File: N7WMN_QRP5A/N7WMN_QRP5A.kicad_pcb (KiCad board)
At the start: 4 copper layers, 159 x 159 mm, 468 parts, among them IC1 SN74CBTLV3253, J1 Conn_01x02, J10 Conn_01x03, J13 Conn_01x02, J14 Conn_01x04, J15 Conn_01x08, J16 Conn_01x03, J17 Conn_01x10, J18 Conn_01x10, J2 Conn_01x02, J3 Conn_01x03, J4 Conn_01x14, J5 AudioJack2_Switch, J6 AudioJack3_Switch, J7 Conn_01x06, J8 Conn_01x02, J9 AudioJack3_Switch, K1 G6SU-2, K2 G6SU-2, K3 G6SU-2, K4 G6SU-2, K5 G6SU-2, K6 G6SU-2, Q1 MMBT3904, Q10 BSS84, Q11 IRF9540, Q2 MMBT3904, Q3 PMV240SP, Q4 MMBT3904, Q44 2N7002, Q5 PMV240SP, Q6 DMN10H220LPDW, Q7 BC847BS, Q9 J309, SW1 SW_Slide_DPDT, T1 T50-TRIFILAR, U1 OPA1679, U10 MIC5235-3.3YM5, U11 LMR51430, U12 UCC27517DBVR, U13 UCC27517DBVR, U14 LMR51430, U15 OPA1679, U16 OPA1679, U17 TS5A3159ADCK, U18 LMC567, U19 TS5A3159ADCK, U2 OPA1678, U20 TS5A3159ADCK, U21 OPA1679, U22 TS5A3159ADCK, U23 LM4810, U24 MIC5235-3.3YM5, U25 MIC5235-3.3YM5, U26 Si5351A-B-GT, U27 L7805ABD2T-TR, U28 OPA1678, U29 OPA1679, U3 TS5A3159ADCK, U30 OPA1678, U31 TS5A3159ADCK, U32 INA821xD, U33 INA821xD, U4 74HCT595, U5 74ACT125, U6 74ACT244, U7 TLV61047DDC, U8 OPA1678, U9 74LVC2G125, Y1 32.768kHz, Y2 25MHz

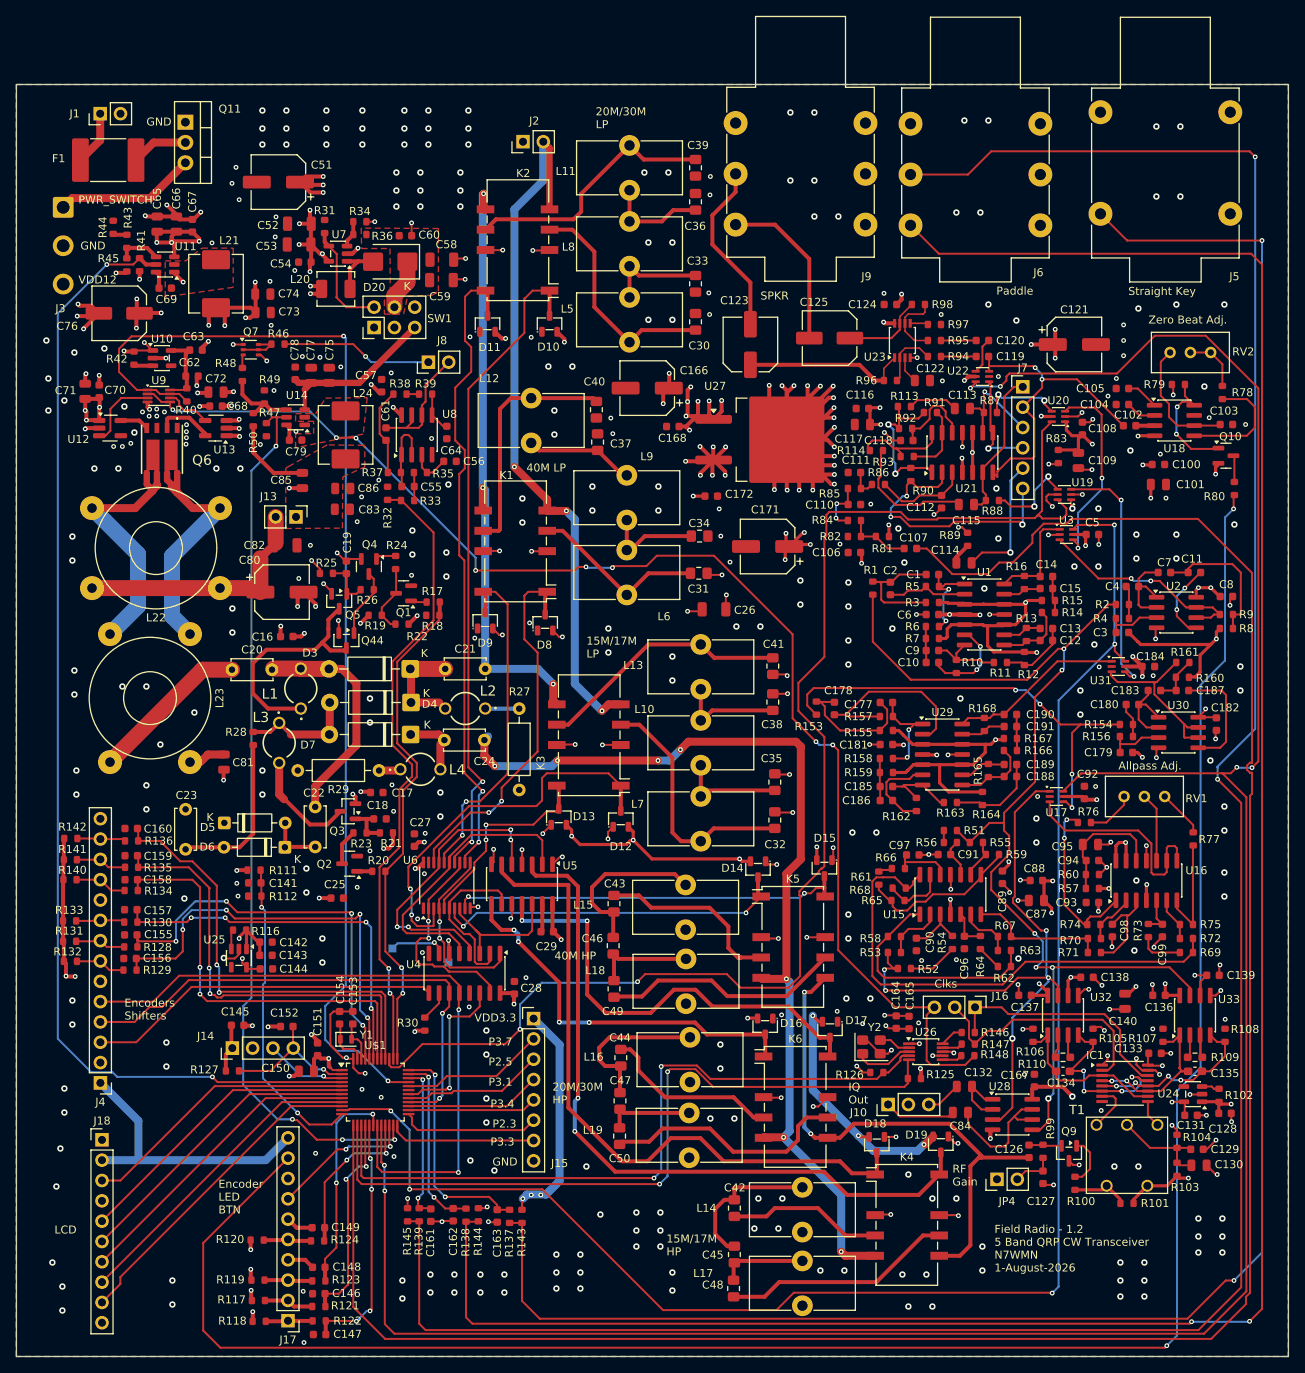
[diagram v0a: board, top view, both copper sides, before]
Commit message: layout update to schematic changes
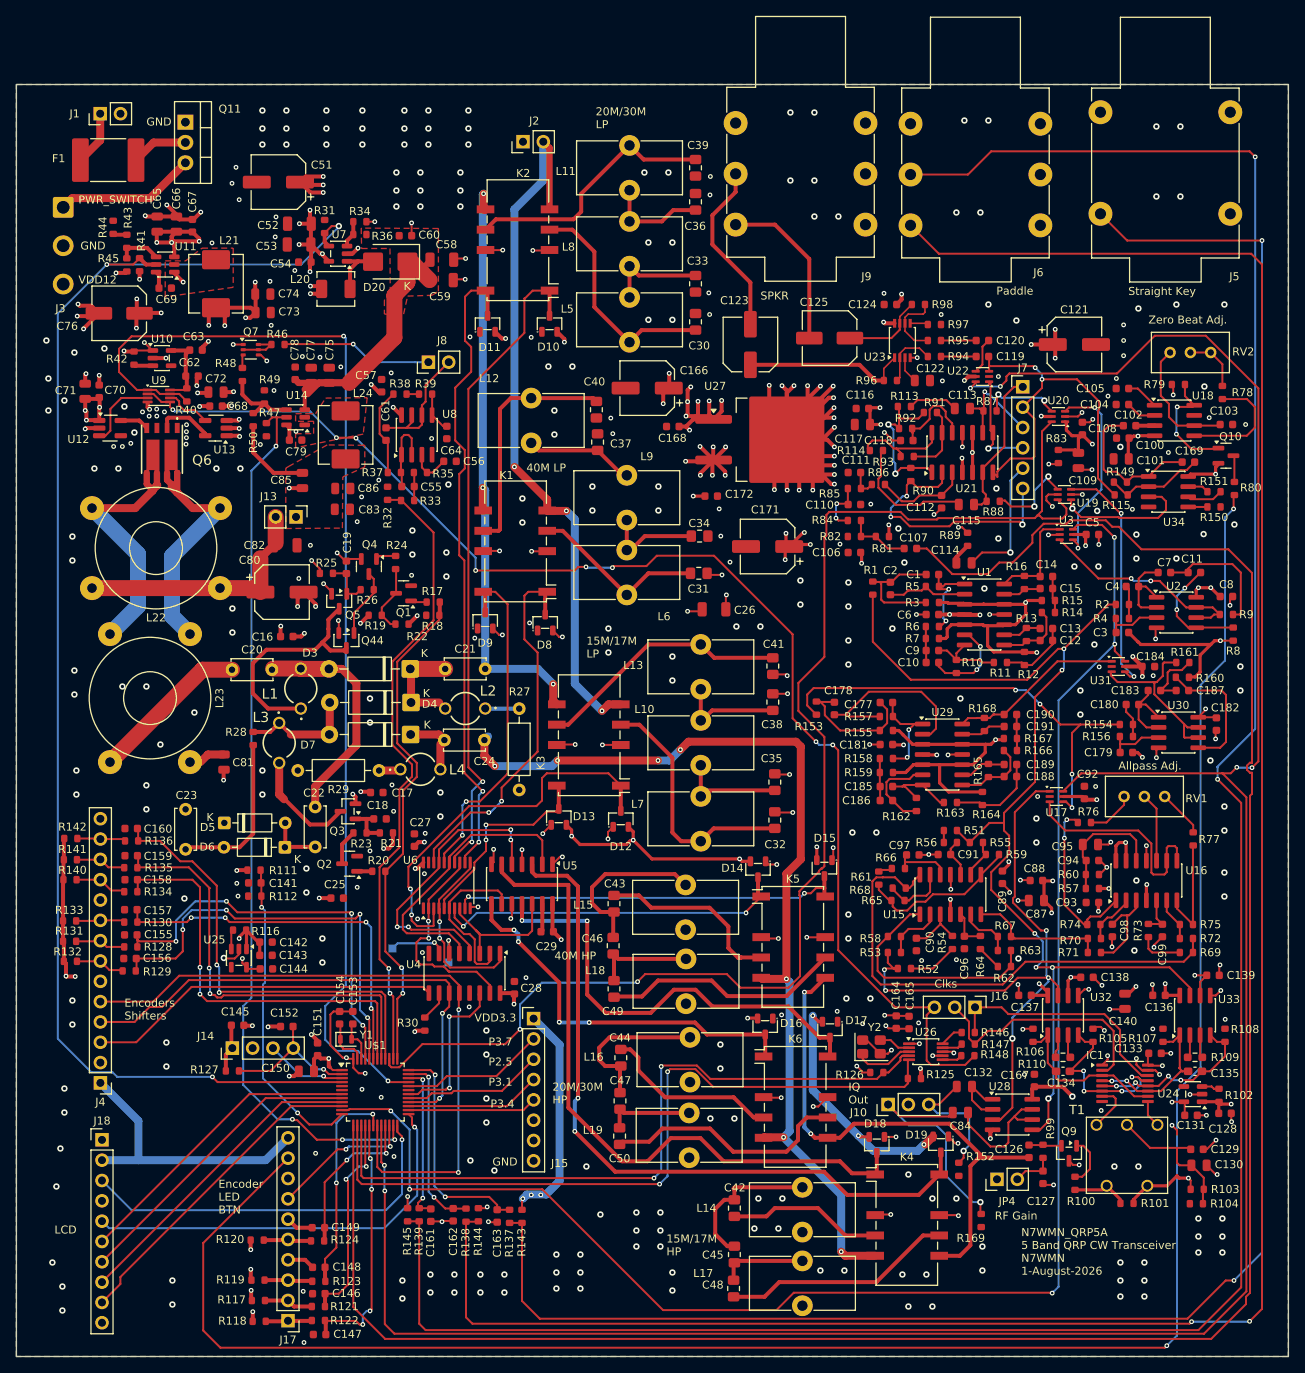
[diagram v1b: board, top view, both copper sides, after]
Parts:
- removed SW1: SW_Slide_DPDT, Connector_PinHeader_2.54mm:PinHeader_2x03_P2.54mm_Vertical
- added C169: 6.8nF, PCM_JLCPCB:C_0603, F.Cu at (218.8, 119.2)
- added R115: 2kΩ, PCM_JLCPCB:R_0603, F.Cu at (210.3, 123.3)
- added R149: 10kΩ, PCM_JLCPCB:R_0603, F.Cu at (210.2, 121.7)
- added R150: 10kΩ, PCM_JLCPCB:R_0603, F.Cu at (221.9, 124.8)
- added R151: 10kΩ, PCM_JLCPCB:R_0603, F.Cu at (221.9, 122.9)
- added R152: 10kΩ, PCM_JLCPCB:R_0603, F.Cu at (190.1, 207.6)
- added R169: 10kΩ, PCM_JLCPCB:R_0603, F.Cu at (192.8, 214.0)
- added U34: OPA1678, Package_SO:SOIC-8_3.9x4.9mm_P1.27mm, F.Cu at (216.2, 122.9)
- R103, R104: value 10kΩ -> 3.3kΩ
- R121, R122, R123, R128, R129, R134, R135: value 39K -> 2kΩ
- R46: value 1kΩ -> 1.8kΩ
- R87, R88: value 10kΩ -> 1kΩ
- moved R104 8.17 mm to (219.8, 211.9), turned to 180 degrees
- moved C101 5.64 mm to (210.3, 118.8), turned to 180 degrees
- moved C100 5.54 mm to (210.6, 116.2), turned to 180 degrees
- moved R103 3.55 mm to (219.8, 210.1), turned to 0 degrees
- moved R8 1.10 mm to (224.3, 140.7), turned to -90 degrees
- moved R87 0.21 mm to (193.9, 112.8)
- moved R134 0.16 mm to (86.5, 172.9)
- moved R129 0.14 mm to (86.3, 182.8)
- moved R88 0.14 mm to (194.3, 124.1)
- moved R135 0.11 mm to (86.5, 169.9)
- moved R122 0.11 mm to (110.0, 226.5)
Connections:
- net /PADDLE_DAH renamed /PADDLE_LEFT
- net /PADDLE_DIT renamed /PADDLE_RIGHT
- C102 pad 2: /Audio/toneDecoder/audio_in -> Net-(C102-Pad2)
- C75 pad 1: /powerAmp/VAMP -> /powerAmp/vbst
- C77 pad 1: /powerAmp/VAMP -> /powerAmp/vbst
- C78 pad 1: /powerAmp/VAMP -> /powerAmp/vbst
- J15 pad 6: /controller/P2.3 -> unconnected-(J15-Pin_6-Pad6)
- J15 pad 7: /controller/P3.3 -> unconnected-(J15-Pin_7-Pad7)
- J4 pad 11: /MEN_ENCODER_A -> /LED_ENCODER_A
- J4 pad 12: /MEN_ENCODER_B -> /LED_ENCODER_B
- J4 pad 13: /MEN_ENCODER_SW -> /LED_ENCODER_SW
- J4 pad 7: /LED_ENCODER_A -> /MENU_ENCODER_A
- J4 pad 8: /LED_ENCODER_B -> /MENU_ENCODER_B
- J4 pad 9: /LED_ENCODER_SW -> /MENU_ENCODER_SW
- R103 pad 1: Net-(C129-Pad2) -> VDD5
- R103 pad 2: VDD5 -> Net-(C129-Pad2)
- R104 pad 1: GND -> Net-(C129-Pad2)
- R104 pad 2: Net-(C129-Pad2) -> GND
- R128 pad 2: /LED_ENCODER_B -> /MENU_ENCODER_B
- R129 pad 2: /LED_ENCODER_A -> /MENU_ENCODER_A
- R130 pad 2: /LED_ENCODER_SW -> /MENU_ENCODER_SW
- R131 pad 2: /LED_ENCODER_B -> /MENU_ENCODER_B
- R132 pad 2: /LED_ENCODER_A -> /MENU_ENCODER_A
- R133 pad 2: /LED_ENCODER_SW -> /MENU_ENCODER_SW
- R134 pad 2: /MEN_ENCODER_A -> /LED_ENCODER_A
- R135 pad 2: /MEN_ENCODER_B -> /LED_ENCODER_B
- R136 pad 2: /MEN_ENCODER_SW -> /LED_ENCODER_SW
- R140 pad 2: /MEN_ENCODER_A -> /LED_ENCODER_A
- R141 pad 2: /MEN_ENCODER_B -> /LED_ENCODER_B
- R142 pad 2: /MEN_ENCODER_SW -> /LED_ENCODER_SW
- R160 pad 1: Net-(C183-Pad1) -> Net-(U30B-+)
- R31 pad 1: Net-(U7-EN) -> /controller/VDD_DRV_ENABLE
- R8 pad 1: Net-(C11-Pad1) -> Net-(U2B-+)
- U$1 pad 24: /controller/P3.3 -> /LCD_RS
- U$1 pad 25: /controller/P2.3 -> /LCD_E
- U$1 pad 5: /LCD_RS -> unconnected-(U$1-P1.5/UCA0RXD/UCA0SOMI/TA1.1/TMS/A5-Pad5)
- U$1 pad 6: /LCD_E -> unconnected-(U$1-P1.6/UCA0CLK/TA1CLK/TDI/TCLK/A6-Pad6)
- U14 pad 3: /powerAmp/VAMP -> /powerAmp/vbst
- U7 pad 4: Net-(U7-EN) -> /controller/VDD_DRV_ENABLE
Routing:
- net /powerAmp/vbst: track 7.00 -> 45.3 mm
- net /controller/VDD_DRV_ENABLE: track 143.9 -> 179.0 mm, vias 2 -> 3
- net /powerAmp/VAMP: track 21.7 -> 0.00 mm
- net Net-(J10-Pin_1): track 8.92 -> 30.0 mm, vias 0 -> 1
- net Net-(C102-Pad2): track 0.00 -> 19.2 mm
- net /controller/P3.3: track 18.3 -> 0.00 mm
- net /controller/P2.3: track 17.5 -> 0.00 mm
- net /Audio/vbias: track 269.4 -> 286.1 mm
- net /LCD_E: track 36.8 -> 52.1 mm, vias 0 -> 1
- net Net-(U7-EN): track 14.0 -> 0.00 mm
- net /LCD_RS: track 34.9 -> 48.7 mm, vias 0 -> 1
- net Net-(U34A--): track 0.00 -> 12.5 mm
- net Net-(J10-Pin_3): track 4.44 -> 16.3 mm, vias 0 -> 1
- net /Audio/toneDecoder/audio_in: track 40.2 -> 48.5 mm
- net /MEN_ENCODER_A: track 6.57 -> 0.00 mm
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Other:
- board text added: "N7WMN_QRP5A 5 Band QRP CW Transceiver N7WMN 1-August-2026"
- board text removed: "Field Radio - 1.2 5 Band QRP CW Transceiver N7WMN 1-August-2026"
- board text removed: "P2.3"
- board text removed: "P3.3"
